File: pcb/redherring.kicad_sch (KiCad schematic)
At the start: 214 parts, among them J2 OLED, SW3 Rotary_Encoder_Switch, U1 ATmega32A-PU, Y1 16Mhz

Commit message: Initianl checkin of blueherring.
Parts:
- removed BOOT1: SW_Push, Button_Switch_THT:SW_PUSH_6mm, symbol Switch:SW_Push
- removed C1, C2: 22pF, Capacitor_THT:C_Disc_D3.0mm_W2.0mm_P2.50mm, symbol Device:C_Small
- removed C3, C4: 0.1uF, Capacitor_THT:C_Disc_D4.3mm_W1.9mm_P5.00mm, symbol Device:C_Small
- removed C5: 4.7uF, Capacitor_THT:CP_Radial_D4.0mm_P1.50mm, symbol Device:C_Small
- removed CAPS1: LED, LED_THT:LED_D3.0mm_Clear, symbol Device:LED
- removed D93, D94: 3.6V, Diode_THT:D_DO-35_SOD27_P7.62mm_Horizontal, symbol Device:D_Zener_Small
- removed F1: 500mA, cftkb:polyfuse_5.1mm, symbol Device:Polyfuse_Small
- removed ISP1: AVR-ISP-6, Connector_PinHeader_2.54mm:PinHeader_2x03_P2.54mm_Vertical, symbol Connector:AVR-ISP-6
- removed R1, R8: 1.5K, Resistor_THT:R_Axial_DIN0204_L3.6mm_D1.6mm_P5.08mm_Horizontal, symbol Device:R_Small
- removed R2, R5: 5.1K, Resistor_THT:R_Axial_DIN0204_L3.6mm_D1.6mm_P5.08mm_Horizontal, symbol Device:R_Small
- removed R3, R4: 75, Resistor_THT:R_Axial_DIN0204_L3.6mm_D1.6mm_P5.08mm_Horizontal, symbol Device:R_Small
- removed R6: 10K, Resistor_THT:R_Axial_DIN0204_L3.6mm_D1.6mm_P5.08mm_Horizontal, symbol Device:R_Small
- removed USB1: USB_C_GCT_USB4085-Type-C, Type-C:USB_C_GCT_USB4085, symbol redherring-rescue:USB_C_GCT_USB4085-Type-C
- removed Y1: 16Mhz, Crystal:Crystal_HC49-4H_Vertical, symbol Device:Crystal_Small
- added U?: Elite-C, symbol keebio:Elite-C
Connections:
- net EN1: now also U?.20 (A3/PF4); no longer U1.24 (PC2)
- net EN2: now also U?.19 (A2/PF5); no longer U1.21 (PD7)
- net SCL: now also U?.6 (3/PD0); no longer U1.22 (PC0)
- net SDA: now also U?.5 (2/PD1); no longer U1.23 (PC1)
- net reset: now also U?.22 (RST); no longer U1.9 (~{RESET})
- net CAPSLOCK: no longer names the net of U1.40 (PA0)
- net D+: no longer names the net of U1.16 (PD2)
- net D-: no longer names the net of U1.17 (PD3)
- net MISO: no longer names the net of U1.7 (PB6)
- net MOSI: no longer names the net of U1.6 (PB5)
- net SCK: no longer names the net of U1.8 (PB7)
- net boot: no longer names the net of U1.18 (PD4)
- no-connect marks 3 -> 1

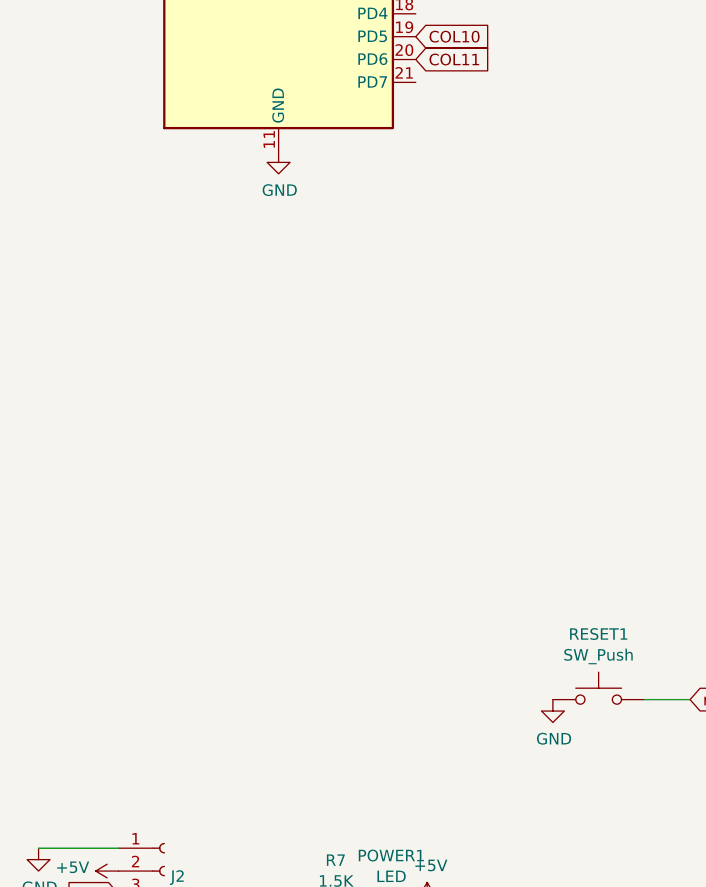
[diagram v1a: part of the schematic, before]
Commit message: Added RPi schema
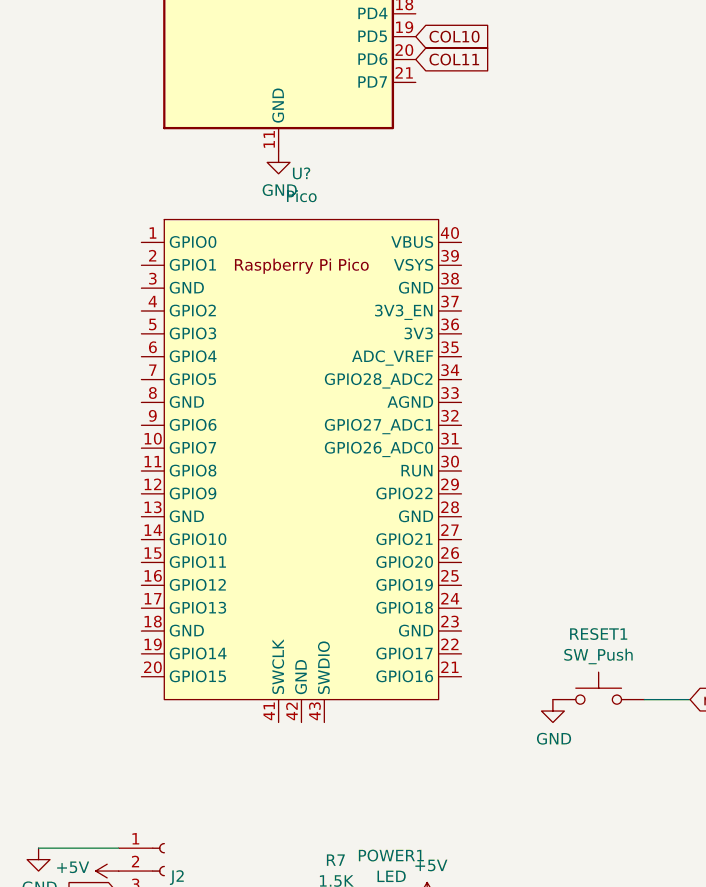
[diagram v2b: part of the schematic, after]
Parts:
- added U?: Pico, RPi_Pico:RPi_Pico_SMD_TH, symbol MCU_RaspberryPi_and_Boards:Pico
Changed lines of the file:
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@@
     (pin "2")
+  )
+  (symbol (lib_id "MCU_RaspberryPi_and_Boards:Pico") (at 55.88 156.21 0) (unit 1)
+    (in_bom yes) (on_board yes) (fields_autoplaced)
+    (property "Reference" "U?" (id 0) (at 55.88 124.46 0))
+    (property "Value" "Pico" (id 1) (at 55.88 127 0))
+    (property "Footprint" "RPi_Pico:RPi_Pico_SMD_TH" (id 2) (at 55.88 156.21 90)
+      (effects (font (size 1.27 1.27)) hide)
+    )
+    (property "Datasheet" "" (id 3) (at 55.88 156.21 0)
+      (effects (font (size 1.27 1.27)) hide)
+    )
+    (pin "1")
+    (pin "10")
+    (pin "11")
+    (pin "12")
+    (pin "13")
+    (pin "14")
+    (pin "15")
+    (pin "16")
+    (pin "17")
+    (pin "18")
+    (pin "19")
+    (pin "2")
+    (pin "20")
+    (pin "21")
+    (pin "22")
+    (pin "23")
+    (pin "24")
+    (pin "25")
+    (pin "26")
+    (pin "27")
+    (pin "28")
+    (pin "29")
+    (pin "3")
+    (pin "30")
+    (pin "31")
+    (pin "32")
+    (pin "33")
+    (pin "34")
+    (pin "35")
+    (pin "36")
+    (pin "37")
+    (pin "38")
+    (pin "39")
+    (pin "4")
+    (pin "40")
+    (pin "41")
+    (pin "42")
+    (pin "43")
+    (pin "5")
+    (pin "6")
+    (pin "7")
+    (pin "8")
+    (pin "9")
   )
   (symbol (lib_id "keebio:Elite-C") (at 196.215 214.63 0) (unit 1)
@@
       (reference "U1") (unit 1) (value "ATmega32A-PU") (footprint "Package_DIP:DIP-40_W15.24mm")
     )
+    (path "/7b5fc8e8-c90e-459f-a15f-2986bff96a70"
+      (reference "U?") (unit 1) (value "Pico") (footprint "RPi_Pico:RPi_Pico_SMD_TH")
+    )
     (path "/b2dfa68c-2499-4458-9ffd-551f1df22680"

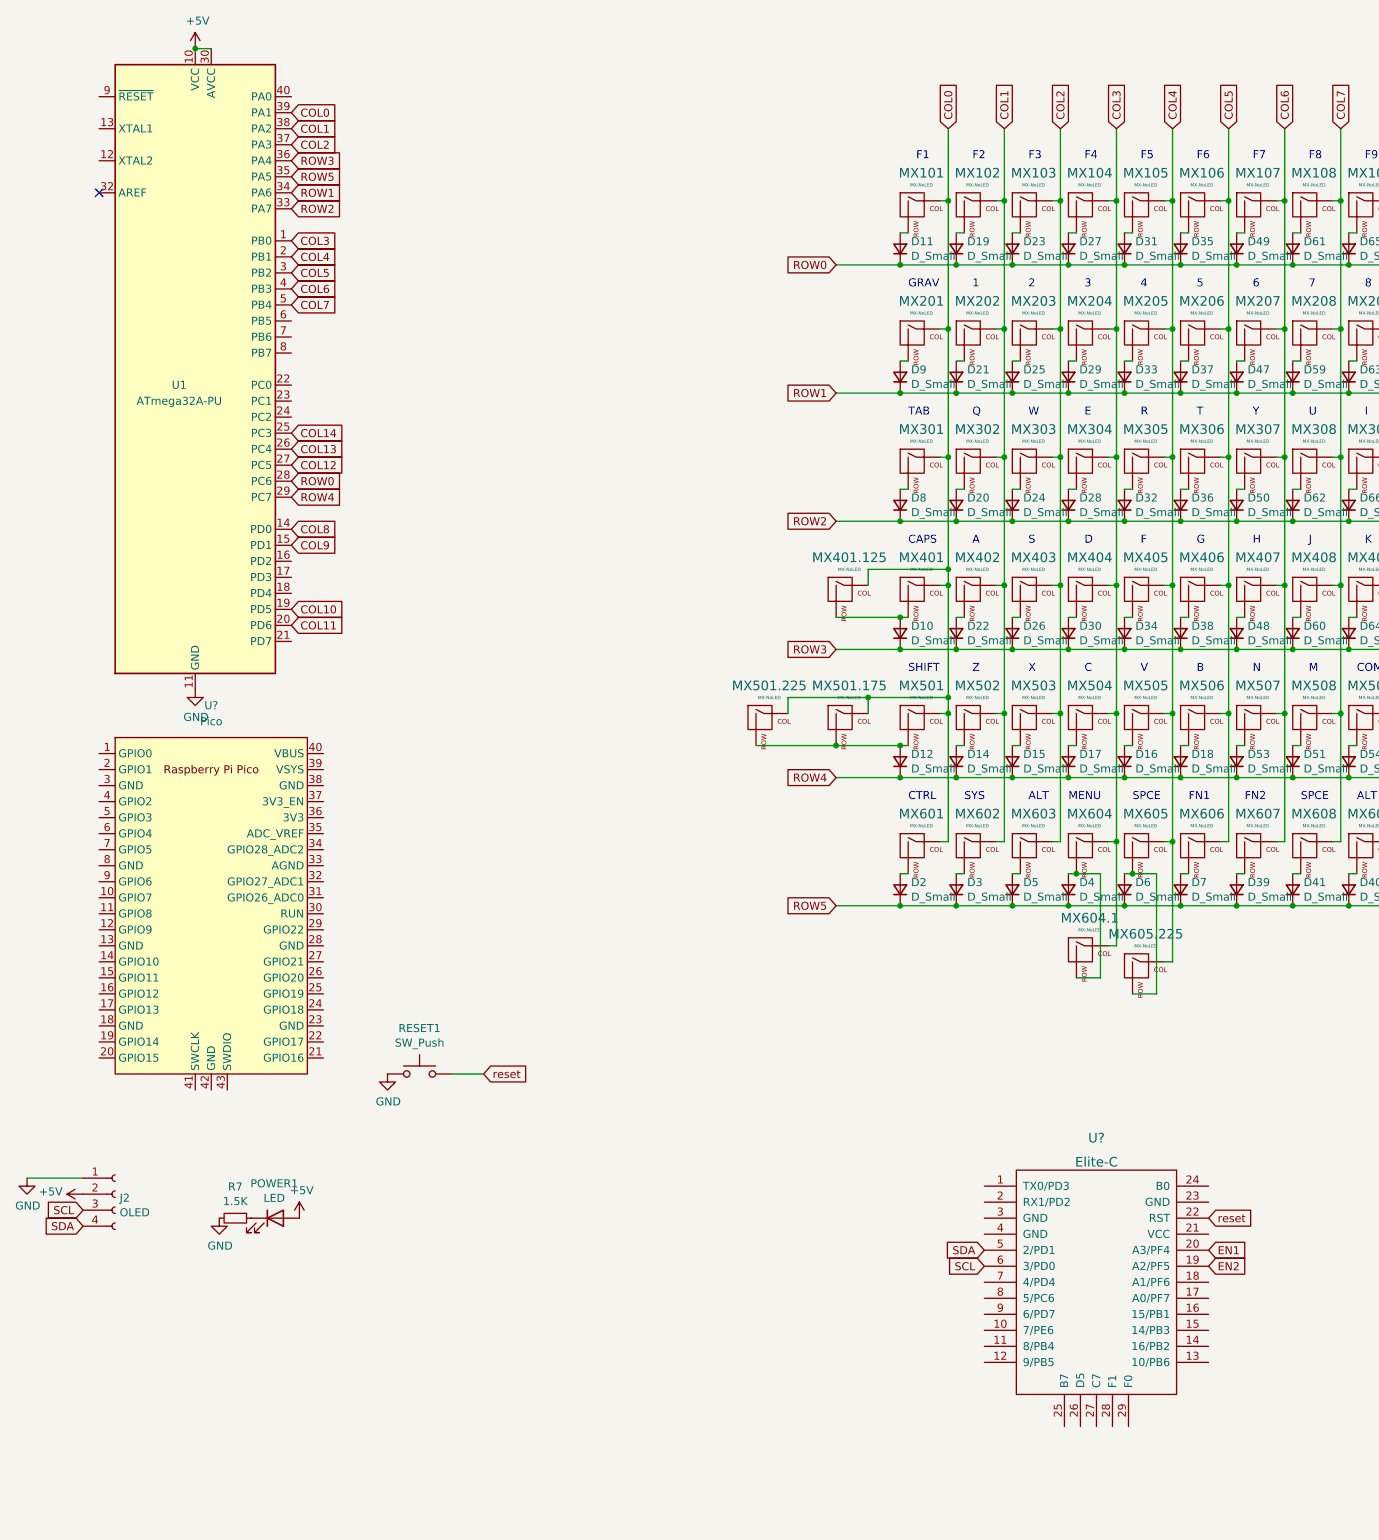
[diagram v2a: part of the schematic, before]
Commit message: Initial reroute to elite-pi instead of individual components.
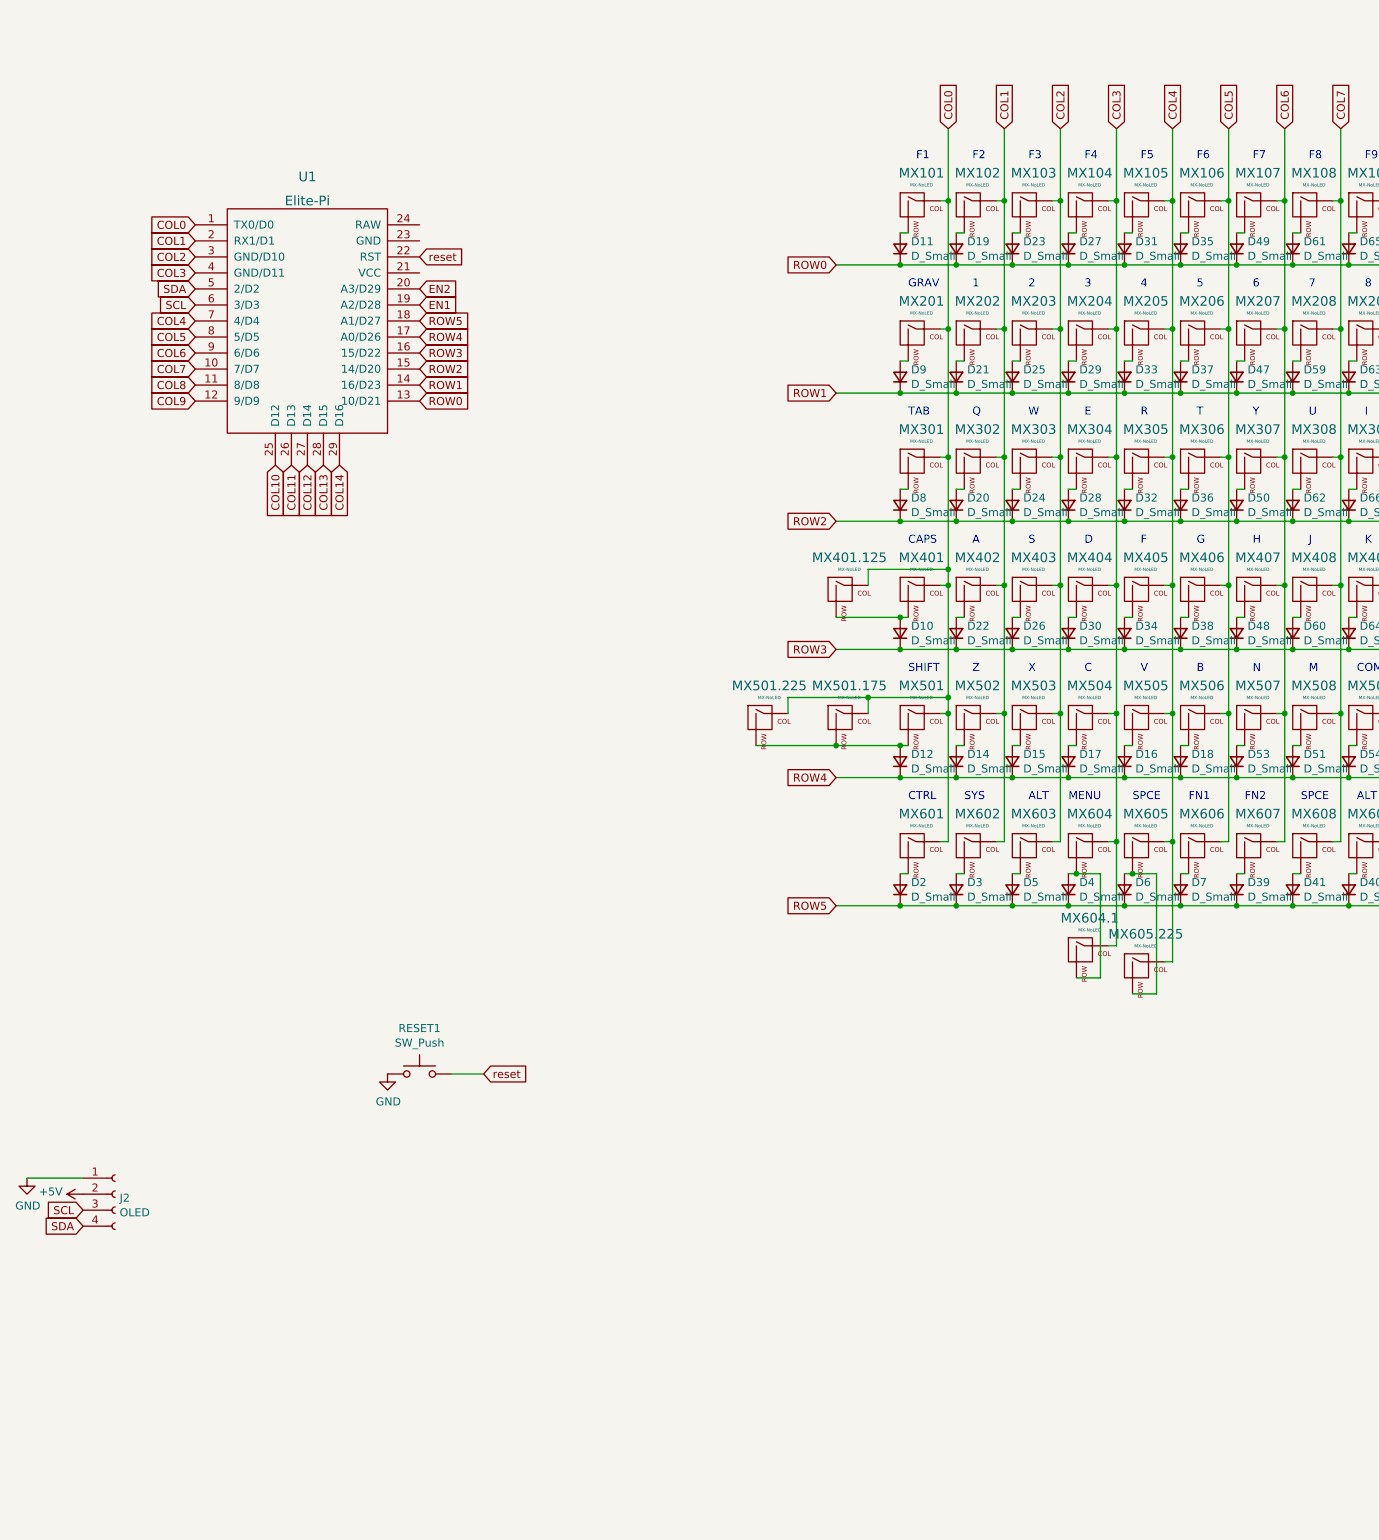
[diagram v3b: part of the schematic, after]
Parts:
- removed POWER1: LED, LED_THT:LED_D3.0mm_Clear, symbol Device:LED
- removed R7: 1.5K, Resistor_THT:R_Axial_DIN0204_L3.6mm_D1.6mm_P5.08mm_Horizontal, symbol Device:R_Small
- removed U1: ATmega32A-PU, Package_DIP:DIP-40_W15.24mm, symbol MCU_Microchip_ATmega:ATmega32A-PU
- removed U?: Pico, RPi_Pico:RPi_Pico_SMD_TH, symbol MCU_RaspberryPi_and_Boards:Pico
- U1: renamed from U?; value Elite-C -> Elite-Pi; footprint (none) -> redherring:Elite-C
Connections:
- net COL0: now also U1.1 (TX0/D0)
- net COL1: now also U1.2 (RX1/D1)
- net COL10: now also U1.25 (D12)
- net COL11: now also U1.26 (D13)
- net COL12: now also U1.27 (D14)
- net COL13: now also U1.28 (D15)
- net COL14: now also U1.29 (D16)
- net COL2: now also U1.3 (GND/D10)
- net COL3: now also U1.4 (GND/D11)
- net COL4: now also U1.7 (4/D4)
- net COL5: now also U1.8 (5/D5)
- net COL6: now also U1.9 (6/D6)
- net COL7: now also U1.10 (7/D7)
- net COL8: now also U1.11 (8/D8)
- net COL9: now also U1.12 (9/D9)
- net EN1: now also U1.19 (A2/D28); no longer U1.20 (A3/PF4)
- net EN2: now also U1.20 (A3/D29); no longer U1.19 (A2/PF5)
- net ROW0: now also U1.13 (10/D21)
- net ROW1: now also U1.14 (16/D23)
- net ROW2: now also U1.15 (14/D20)
- net ROW3: now also U1.16 (15/D22)
- net ROW4: now also U1.17 (A0/D26)
- net ROW5: now also U1.18 (A1/D27)
- no-connect marks 1 -> 0
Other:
- moved on the sheet: U1
